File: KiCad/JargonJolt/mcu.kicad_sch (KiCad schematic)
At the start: 34 parts, among them J1 Conn_01x05, Q1 SS8050-G, Q2 SS8050-G, SW1 SW_Push, SW2 SW_Push, U1 ESP32-S3-WROOM-1-N16R2

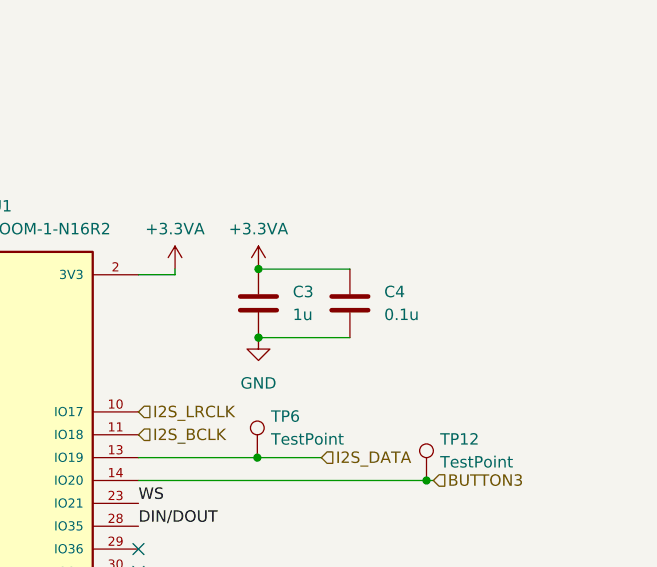
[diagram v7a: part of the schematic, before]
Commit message: added 3.3v test led
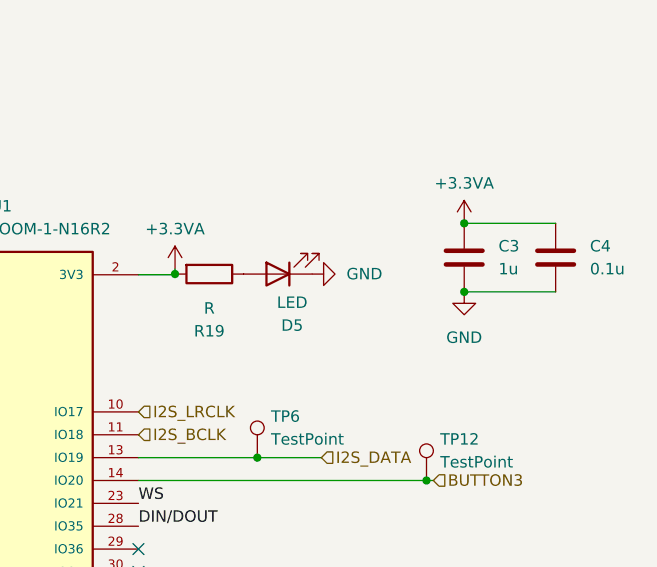
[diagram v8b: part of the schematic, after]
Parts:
- added D5: LED, LED_SMD:LED_1206_3216Metric_Pad1.42x1.75mm_HandSolder, symbol Device:LED
- added R19: R, Resistor_SMD:R_0805_2012Metric, symbol Device:R
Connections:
- net +3.3VA: now also R19.2
- net GND: now also D5.1 (K)
- new net: D5.2 (A), R19.1
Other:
- moved on the sheet: C3, C4
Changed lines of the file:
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@@
   (junction (at 50.8 47.625) (diameter 0) (color 0 0 0 0)
   )
-  (junction (at 215.9 54.61) (diameter 0) (color 0 0 0 0)
+  (junction (at 238.76 49.53) (diameter 0) (color 0 0 0 0)
   )
   (junction (at 219.202 98.425) (diameter 0) (color 0 0 0 0)
@@
   (junction (at 219.202 100.965) (diameter 0) (color 0 0 0 0)
   )
+  (junction (at 206.629 55.1671) (diameter 0) (color 0 0 0 0)
+  )
   (junction (at 52.705 70.485) (diameter 0) (color 0 0 0 0)
   )
-  (junction (at 215.9 62.23) (diameter 0) (color 0 0 0 0)
+  (junction (at 238.76 57.15) (diameter 0) (color 0 0 0 0)
   )
   (junction (at 50.8 37.465) (diameter 0) (color 0 0 0 0)
@@
     (stroke (width 0) (type default))
   )
-  (wire (pts (xy 206.629 54.61) (xy 206.629 55.245))
+  (wire (pts (xy 206.629 54.61) (xy 206.629 55.1671))
     (stroke (width 0) (type default))
   )
@@
   )
   (wire (pts (xy 90.805 116.84) (xy 90.805 114.3))
+    (stroke (width 0) (type default))
+  )
+  (wire (pts (xy 206.629 55.1671) (xy 206.629 55.245))
     (stroke (width 0) (type default))
   )
@@
     (stroke (width 0) (type default))
   )
-  (wire (pts (xy 215.9 54.61) (xy 226.06 54.61))
+  (wire (pts (xy 238.76 49.53) (xy 248.92 49.53))
     (stroke (width 0) (type default))
   )
@@
     (stroke (width 0) (type default))
   )
-  (wire (pts (xy 215.9 62.23) (xy 226.06 62.23))
+  (wire (pts (xy 238.76 57.15) (xy 248.92 57.15))
     (stroke (width 0) (type default))
   )
@@
     )
   )
-  (symbol (lib_id "power:+3.3VA") (at 215.9 54.61 0) (unit 1)
-    (in_bom yes) (on_board yes) (dnp no) (fields_autoplaced)
-    (property "Reference" "#PWR011" (at 215.9 58.42 0)
-      (effects (font (size 1.27 1.27)) hide)
-    )
-    (property "Value" "+3.3VA" (at 215.9 50.165 0)
-      (effects (font (size 1.27 1.27)))
-    )
-    (property "Footprint" "" (at 215.9 54.61 0)
-      (effects (font (size 1.27 1.27)) hide)
-    )
-    (property "Datasheet" "" (at 215.9 54.61 0)
+  (symbol (lib_id "power:+3.3VA") (at 238.76 49.53 0) (unit 1)
+    (in_bom yes) (on_board yes) (dnp no) (fields_autoplaced)
+    (property "Reference" "#PWR011" (at 238.76 53.34 0)
+      (effects (font (size 1.27 1.27)) hide)
+    )
+    (property "Value" "+3.3VA" (at 238.76 45.085 0)
+      (effects (font (size 1.27 1.27)))
+    )
+    (property "Footprint" "" (at 238.76 49.53 0)
+      (effects (font (size 1.27 1.27)) hide)
+    )
+    (property "Datasheet" "" (at 238.76 49.53 0)
       (effects (font (size 1.27 1.27)) hide)
     )
@@
     )
   )
-  (symbol (lib_id "Device:C") (at 226.06 58.42 0) (unit 1)
-    (in_bom yes) (on_board yes) (dnp no) (fields_autoplaced)
-    (property "Reference" "C4" (at 229.87 57.15 0)
-      (effects (font (size 1.27 1.27)) (justify left))
-    )
-    (property "Value" "0.1u" (at 229.87 59.69 0)
-      (effects (font (size 1.27 1.27)) (justify left))
-    )
-    (property "Footprint" "Capacitor_SMD:C_0805_2012Metric" (at 227.0252 62.23 0)
-      (effects (font (size 1.27 1.27)) hide)
-    )
-    (property "Datasheet" "~" (at 226.06 58.42 0)
+  (symbol (lib_id "Device:C") (at 248.92 53.34 0) (unit 1)
+    (in_bom yes) (on_board yes) (dnp no) (fields_autoplaced)
+    (property "Reference" "C4" (at 252.73 52.07 0)
+      (effects (font (size 1.27 1.27)) (justify left))
+    )
+    (property "Value" "0.1u" (at 252.73 54.61 0)
+      (effects (font (size 1.27 1.27)) (justify left))
+    )
+    (property "Footprint" "Capacitor_SMD:C_0805_2012Metric" (at 249.8852 57.15 0)
+      (effects (font (size 1.27 1.27)) hide)
+    )
+    (property "Datasheet" "~" (at 248.92 53.34 0)
       (effects (font (size 1.27 1.27)) hide)
     )
@@
         (path "/39fa52d1-bab8-41e3-aba2-e2f783adaf1f/f670ffa6-f5d6-4e9f-b184-650db4d3a97d"
           (reference "R7") (unit 1)
+        )
+      )
+    )
+  )
+  (symbol (lib_id "power:GND") (at 221.869 55.1671 90) (unit 1)
+    (in_bom yes) (on_board yes) (dnp no) (fields_autoplaced)
+    (property "Reference" "#PWR054" (at 228.219 55.1671 0)
+      (effects (font (size 1.27 1.27)) hide)
+    )
+    (property "Value" "GND" (at 225.679 55.1671 90)
+      (effects (font (size 1.27 1.27)) (justify right))
+    )
+    (property "Footprint" "" (at 221.869 55.1671 0)
+      (effects (font (size 1.27 1.27)) hide)
+    )
+    (property "Datasheet" "" (at 221.869 55.1671 0)
+      (effects (font (size 1.27 1.27)) hide)
+    )
+    (pin "1")
+    (instances
+      (project "JargonJolt"
+        (path "/39fa52d1-bab8-41e3-aba2-e2f783adaf1f/f670ffa6-f5d6-4e9f-b184-650db4d3a97d"
+          (reference "#PWR054") (unit 1)
         )
       )
@@
     )
   )
+  (symbol (lib_id "Device:LED") (at 218.059 55.1671 180) (unit 1)
+    (in_bom yes) (on_board yes) (dnp no) (fields_autoplaced)
+    (property "Reference" "D5" (at 219.6465 60.8821 0)
+      (effects (font (size 1.27 1.27)))
+    )
+    (property "Value" "LED" (at 219.6465 58.3421 0)
+      (effects (font (size 1.27 1.27)))
+    )
+    (property "Footprint" "LED_SMD:LED_1206_3216Metric_Pad1.42x1.75mm_HandSolder" (at 218.059 55.1671 0)
+      (effects (font (size 1.27 1.27)) hide)
+    )
+    (property "Datasheet" "~" (at 218.059 55.1671 0)
+      (effects (font (size 1.27 1.27)) hide)
+    )
+    (pin "2")
+    (pin "1")
+    (instances
+      (project "JargonJolt"
+        (path "/39fa52d1-bab8-41e3-aba2-e2f783adaf1f/f670ffa6-f5d6-4e9f-b184-650db4d3a97d"
+          (reference "D5") (unit 1)
+        )
+      )
+    )
+  )
   (symbol (lib_id "Device:C") (at 52.705 74.295 0) (unit 1)
     (in_bom yes) (on_board yes) (dnp no) (fields_autoplaced)
@@
     )
   )
-  (symbol (lib_id "Device:C") (at 215.9 58.42 0) (unit 1)
-    (in_bom yes) (on_board yes) (dnp no) (fields_autoplaced)
-    (property "Reference" "C3" (at 219.71 57.15 0)
-      (effects (font (size 1.27 1.27)) (justify left))
-    )
-    (property "Value" "1u" (at 219.71 59.69 0)
-      (effects (font (size 1.27 1.27)) (justify left))
-    )
-    (property "Footprint" "Capacitor_SMD:C_0805_2012Metric" (at 216.8652 62.23 0)
-      (effects (font (size 1.27 1.27)) hide)
-    )
-    (property "Datasheet" "~" (at 215.9 58.42 0)
+  (symbol (lib_id "Device:C") (at 238.76 53.34 0) (unit 1)
+    (in_bom yes) (on_board yes) (dnp no) (fields_autoplaced)
+    (property "Reference" "C3" (at 242.57 52.07 0)
+      (effects (font (size 1.27 1.27)) (justify left))
+    )
+    (property "Value" "1u" (at 242.57 54.61 0)
+      (effects (font (size 1.27 1.27)) (justify left))
+    )
+    (property "Footprint" "Capacitor_SMD:C_0805_2012Metric" (at 239.7252 57.15 0)
+      (effects (font (size 1.27 1.27)) hide)
+    )
+    (property "Datasheet" "~" (at 238.76 53.34 0)
       (effects (font (size 1.27 1.27)) hide)
     )
@@
         (path "/39fa52d1-bab8-41e3-aba2-e2f783adaf1f/f670ffa6-f5d6-4e9f-b184-650db4d3a97d"
           (reference "#PWR06") (unit 1)
+        )
+      )
+    )
+  )
+  (symbol (lib_id "Device:R") (at 210.439 55.1671 270) (unit 1)
+    (in_bom yes) (on_board yes) (dnp no) (fields_autoplaced)
+    (property "Reference" "R19" (at 210.439 61.5171 90)
+      (effects (font (size 1.27 1.27)))
+    )
+    (property "Value" "R" (at 210.439 58.9771 90)
+      (effects (font (size 1.27 1.27)))
+    )
+    (property "Footprint" "Resistor_SMD:R_0805_2012Metric" (at 210.439 53.3891 90)
+      (effects (font (size 1.27 1.27)) hide)
+    )
+    (property "Datasheet" "~" (at 210.439 55.1671 0)
+      (effects (font (size 1.27 1.27)) hide)
+    )
+    (pin "2")
+    (pin "1")
+    (instances
+      (project "JargonJolt"
+        (path "/39fa52d1-bab8-41e3-aba2-e2f783adaf1f/f670ffa6-f5d6-4e9f-b184-650db4d3a97d"
+          (reference "R19") (unit 1)
         )
       )
@@
     )
   )
-  (symbol (lib_id "power:GND") (at 215.9 62.23 0) (unit 1)
-    (in_bom yes) (on_board yes) (dnp no) (fields_autoplaced)
-    (property "Reference" "#PWR012" (at 215.9 68.58 0)
-      (effects (font (size 1.27 1.27)) hide)
-    )
-    (property "Value" "GND" (at 215.9 67.31 0)
-      (effects (font (size 1.27 1.27)))
-    )
-    (property "Footprint" "" (at 215.9 62.23 0)
-      (effects (font (size 1.27 1.27)) hide)
-    )
-    (property "Datasheet" "" (at 215.9 62.23 0)
-      (effects (font (size 1.27 1.27)) hide)
-    )
+  (symbol (lib_id "power:GND") (at 238.76 57.15 0) (unit 1)
+    (in_bom yes) (on_board yes) (dnp no) (fields_autoplaced)
+    (property "Reference" "#PWR012" (at 238.76 63.5 0)
+      (effects (font (size 1.27 1.27)) hide)
+    )
+    (property "Value" "GND" (at 238.76 62.23 0)
+      (effects (font (size 1.27 1.27)))
+    )
+    (property "Footprint" "" (at 238.76 57.15 0)
+      (effects (font (size 1.27 1.27)) hide)
+    )
+    (property "Datasheet" "" (at 238.76 57.15 0)
+      (effects (font (size 1.27 1.27)) hide)
+    )
